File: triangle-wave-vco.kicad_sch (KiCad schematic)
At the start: 18 parts, among them J1 Conn_Coaxial, J2 Conn_Coaxial, J3 Conn_01x01, J4 Conn_01x01, Q1 2N3904, U1 LM358

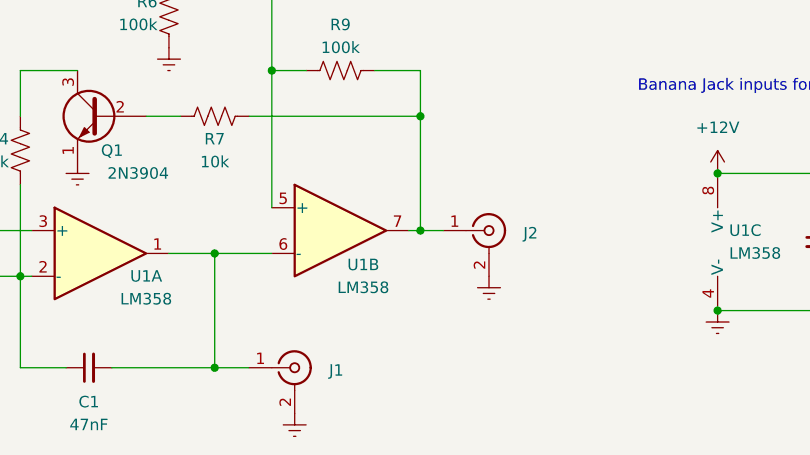
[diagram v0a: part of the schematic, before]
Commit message: Update schematic and change file names to match new repository name.
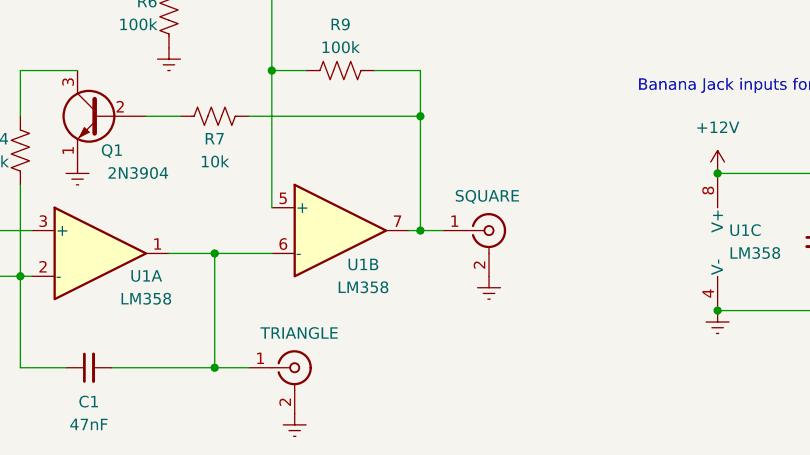
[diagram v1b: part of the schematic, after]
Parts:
- renumbered J2 to SQUARE, J1 to TRIANGLE
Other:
- title: LM358 VCO -> Triangle Wave VCO (LM358)
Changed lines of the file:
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@@
   (paper "A5")
   (title_block
-    (title "LM358 VCO")
-    (date "2023-06-21")
+    (title "Triangle Wave VCO (LM358)")
+    (date "2023-07-14")
     (company "Newell Jensen")
   )
@@
   )
   (symbol (lib_id "Connector:Conn_Coaxial") (at 99.06 83.82 0) (unit 1)
-    (in_bom yes) (on_board yes) (fields_autoplaced)
-    (property "Reference" "J1" (id 0) (at 102.87 84.1131 0)
+    (in_bom yes) (on_board yes)
+    (property "Reference" "TRIANGLE" (id 0) (at 95.25 80.01 0)
       (effects (font (size 1.27 1.27)) (justify left))
     )
@@
   )
   (symbol (lib_id "Connector:Conn_Coaxial") (at 120.65 68.58 0) (unit 1)
-    (in_bom yes) (on_board yes) (fields_autoplaced)
-    (property "Reference" "J2" (id 0) (at 124.46 68.8731 0)
+    (in_bom yes) (on_board yes)
+    (property "Reference" "SQUARE" (id 0) (at 116.84 64.77 0)
       (effects (font (size 1.27 1.27)) (justify left))
     )
@@
       (reference "C2") (unit 1) (value "0.1uF") (footprint "Capacitor_SMD:C_0805_2012Metric")
     )
-    (path "/6f75b3d2-6573-47a6-9a81-a8a8fb9b4649"
-      (reference "J1") (unit 1) (value "Conn_Coaxial") (footprint "Connector_Wire:SolderWire-0.25sqmm_1x02_P4.5mm_D0.65mm_OD2mm")
-    )
-    (path "/b9e63450-1b09-4482-9eb6-861b27c2015a"
-      (reference "J2") (unit 1) (value "Conn_Coaxial") (footprint "Connector_Wire:SolderWire-0.25sqmm_1x02_P4.5mm_D0.65mm_OD2mm")
-    )
     (path "/759c0c56-9333-4544-bd98-00d7f2aec493"
       (reference "J3") (unit 1) (value "Conn_01x01") (footprint "Connector_Wire:SolderWire-0.25sqmm_1x01_D0.65mm_OD2mm")
@@
       (reference "RV1") (unit 1) (value "20k") (footprint "Potentiometer_THT:Potentiometer_Alps_RK163_Single_Horizontal")
     )
+    (path "/b9e63450-1b09-4482-9eb6-861b27c2015a"
+      (reference "SQUARE") (unit 1) (value "Conn_Coaxial") (footprint "Connector_Wire:SolderWire-0.25sqmm_1x02_P4.5mm_D0.65mm_OD2mm")
+    )
+    (path "/6f75b3d2-6573-47a6-9a81-a8a8fb9b4649"
+      (reference "TRIANGLE") (unit 1) (value "Conn_Coaxial") (footprint "Connector_Wire:SolderWire-0.25sqmm_1x02_P4.5mm_D0.65mm_OD2mm")
+    )
     (path "/e7de4123-128b-4c12-b6fc-9c25cca43509"
